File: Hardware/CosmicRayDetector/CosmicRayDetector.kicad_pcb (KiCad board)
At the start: 2 copper layers, 100 x 70 mm, 35 parts, among them J1 USB_B_Micro, J2 Conn_01x01_Female, J3 Conn_01x01_Female, J4 Conn_01x01_Female, J5 Conn_01x01_Female, J6 Conn_01x04, J7 Conn_01x02, U1 HEF4093B, U2 MCP73831-5-OT

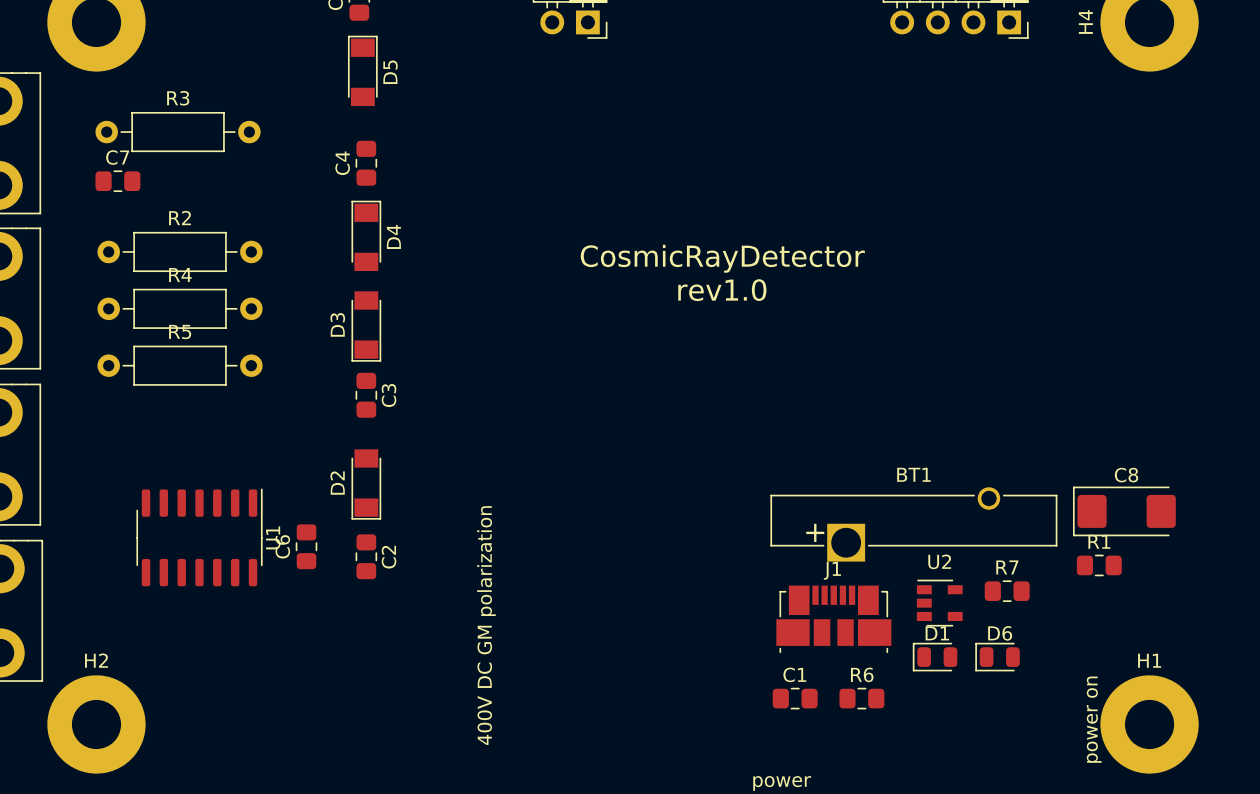
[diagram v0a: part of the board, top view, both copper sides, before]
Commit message: fix #54, fix: #84
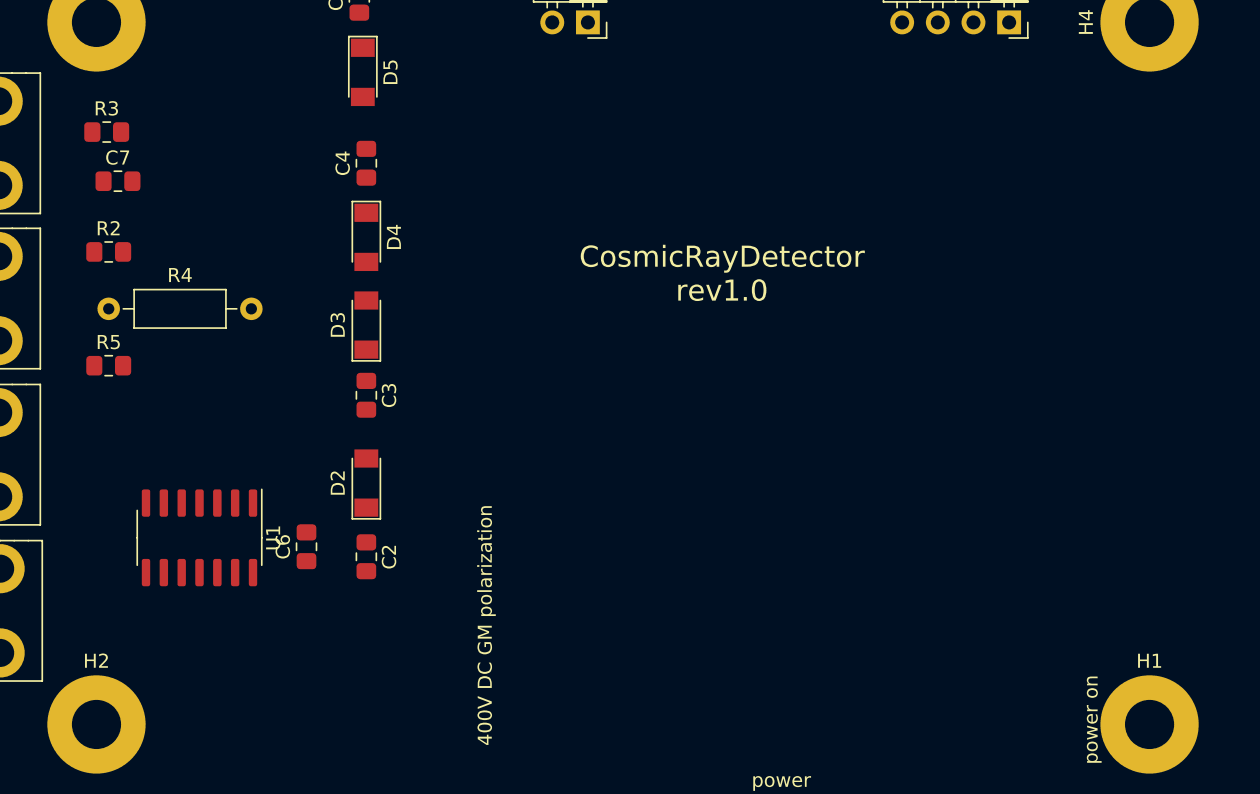
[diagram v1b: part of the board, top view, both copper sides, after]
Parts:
- removed BT1: Battery_Cell, Battery:Battery_Panasonic_CR2025-V1AK_Vertical_CircularHoles
- removed C1: 100n, Capacitor_SMD:C_0805_2012Metric_Pad1.15x1.40mm_HandSolder
- removed C8: 10u, Capacitor_Tantalum_SMD:CP_EIA-6032-28_Kemet-C
- removed D1, D6: red, LED_SMD:LED_0805_2012Metric
- removed J1: USB_B_Micro, Connector_USB:USB_Micro-B_Molex_47346-0001
- removed R1: 520R, Resistor_SMD:R_0805_2012Metric_Pad1.15x1.40mm_HandSolder
- removed R6: 2k2, Resistor_SMD:R_0805_2012Metric_Pad1.15x1.40mm_HandSolder
- removed R7: 470R, Resistor_SMD:R_0805_2012Metric_Pad1.15x1.40mm_HandSolder
- removed U2: MCP73831-5-OT, Package_TO_SOT_SMD:SOT-23-5
- R2, R3, R5: footprint Resistor_THT:R_Axial_DIN0207_L6.3mm_D2.5mm_P10.16mm_Horizontal -> Resistor_SMD:R_0805_2012Metric_Pad1.15x1.40mm_HandSolder
